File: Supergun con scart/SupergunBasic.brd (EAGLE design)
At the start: 114.9 x 67.3 mm, 37 parts, among them J1 AUDIO_JACK_3.5MM_PTH, X2 SCART-F

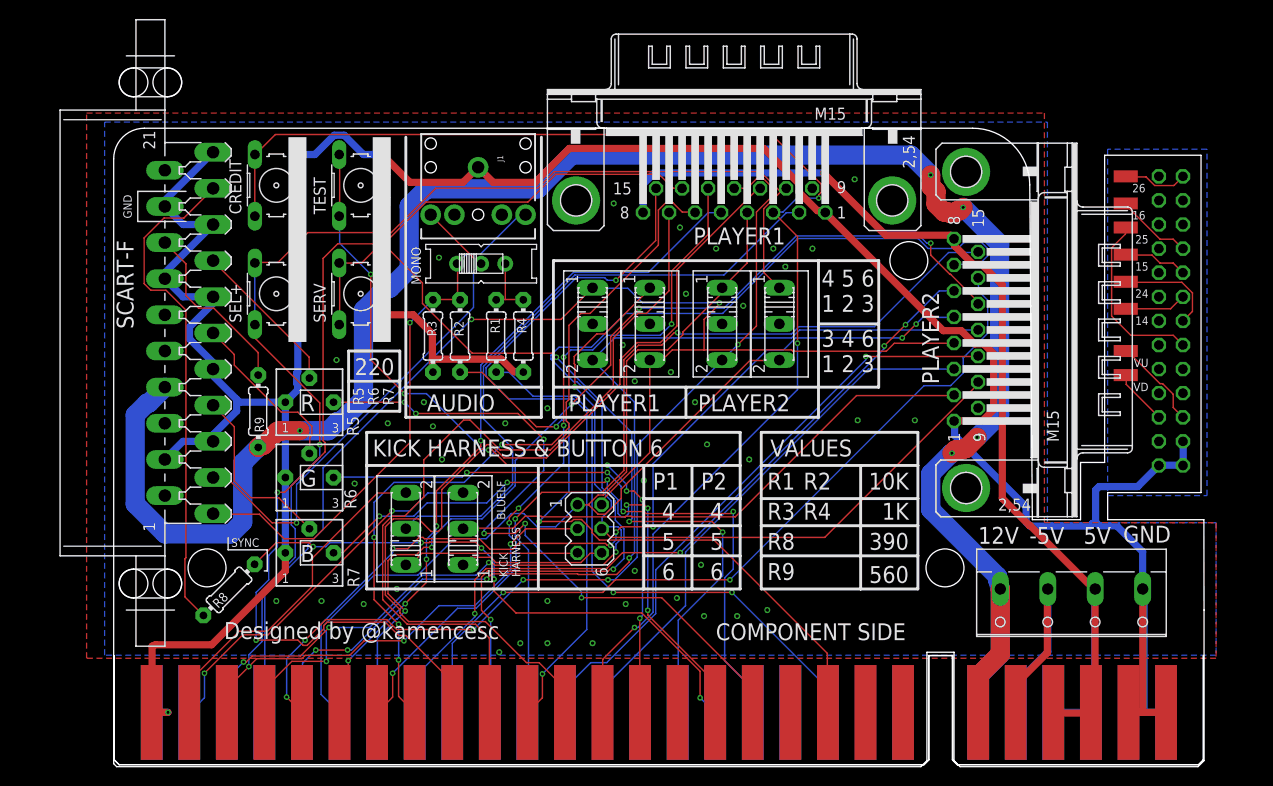
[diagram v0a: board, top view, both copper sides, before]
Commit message: Add files via upload
Actualizados sch y brd.

En el esquema se han icluïdo 2 subplacas que tienen que cortarse. Estas subplacas permiten conectarse al Kick Harness de CPS2. La pequeña va conectada a la Supergun (simplemente hacer coincidir los 2 circulos dibujados en una esquita del pinheader) y el grande va al connector Kick Harness de CPS2. Este incluye Vol+ y Vol- pero la supergun no se ha dado compatibilidad, por lo tanto estan para poder cablearos a unos swtich externos. Para usarlo simplemente asegurarse que el pin que señala la flecha es el de abajo la derecha al enchufarlo.
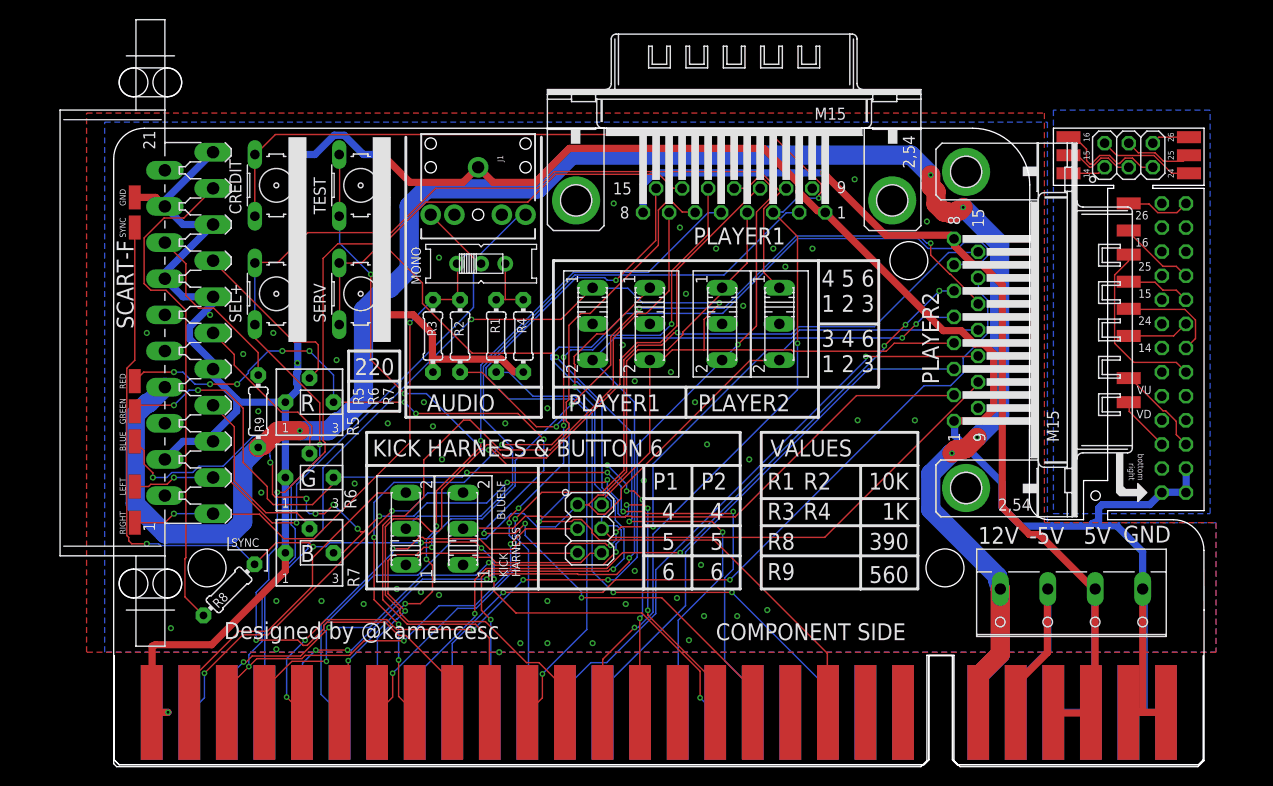
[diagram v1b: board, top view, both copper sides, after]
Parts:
- removed KH_CPS2: (no value), con-lstb:MA03-2
- added 1, 2, 3, 4, 5, 6, PAD1, PAD2, PAD3, PAD4, PAD5, PAD7, PAD8: (no value), wirepad:SMD1,27-2,54
- added JP2, JP3: (no value), pinhead:2X03
- moved JP1 2.88 mm to (111.8, 44.1)
- moved 15 2.88 mm to (107.0, 51.1)
- moved 16 2.88 mm to (107.0, 56.5)
- moved 24 2.88 mm to (107.0, 48.3)
- moved 25 2.88 mm to (107.0, 54.0)
- moved VD 2.88 mm to (107.0, 38.4)
- moved 14 2.88 mm to (107.0, 45.4)
- moved 26 2.88 mm to (107.0, 59.4)
- moved VU 2.88 mm to (107.0, 41.0)
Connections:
- new net K_14: 1.1, JP2.1
- new net K_15: 2.1, JP2.3
- new net K_16: 3.1, JP2.5
- new net K_24: 6.1, JP2.2
- new net K_25: 5.1, JP2.4
- new net K_26: 4.1, JP2.6
- net AUDIO_LEFT: now also PAD7.1
- net AUDIO_RIGHT: now also PAD8.1
- net GND: now also PAD5.1
- net J_BLUE: now also PAD3.1
- net J_GREEN: now also PAD2.1
- net J_RED: now also PAD1.1
- net J_SYNC: now also PAD4.1
- net K_P1_B6: now also JP3.5; no longer KH_CPS2.5
- net K_P2_B6: now also JP3.6; no longer KH_CPS2.6
- net P1_B4: now also JP3.1; no longer KH_CPS2.1
- net P1_B5: now also JP3.3; no longer KH_CPS2.3
- net P2_B4: now also JP3.2; no longer KH_CPS2.2
- net P2_B5: now also JP3.4; no longer KH_CPS2.4
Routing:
- net J_SYNC: track 60.8 -> 108.6 mm, vias 5 -> 6
- net J_BLUE: track 65.4 -> 102.8 mm, vias 6 -> 12
- net J_GREEN: track 68.5 -> 101.0 mm, vias 4 -> 6
- net J_RED: track 75.9 -> 103.2 mm, vias 6 -> 11
- net K_16: track 0.00 -> 12.1 mm
- net K_24: track 0.00 -> 10.2 mm
- net AUDIO_RIGHT: track 58.4 -> 67.1 mm, vias 1 -> 2
- net AUDIO_LEFT: track 53.7 -> 62.3 mm, vias 1 -> 2
- net K_15: track 0.00 -> 7.68 mm
- net K_25: track 0.00 -> 7.40 mm
- net K_26: track 0.00 -> 4.07 mm
- net K_14: track 0.00 -> 4.07 mm
- net GND: track 350.1 -> 352.3 mm, vias 44 -> 57
- net S_RED: track 16.6 -> 18.7 mm
- net P1_B2: track 74.8 -> 76.2 mm
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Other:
- outline, holes or cut-outs redrawn
- board text added: "14"
- board text added: "15"
- board text added: "16"
- board text added: "24"
- board text added: "25"
- board text added: "26"
- board text added: "BLUE"
- board text added: "Basic Supergun + Scart v 0.1 test"
- board text added: "GREEN"
- board text added: "LEFT"
- board text added: "RED"
- board text added: "RIGHT"
- board text added: "This side faces to the board"
- board text added: "bottom"
- board text added: "right"
- board text removed: "Basic Supergun"

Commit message: Add files via upload
Actualización
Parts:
- removed MO_ST: (no value), adafruit:EG1218
- removed PAD1, PAD2, PAD3, PAD4, PAD5, PAD7, PAD8: (no value), wirepad:SMD1,27-2,54
- removed S2, S3, S5, S6: (no value), switch:255SB
- removed X2: SCART-F, con-hirschmann:SCART-F
- added AUDIO, SYNC_G: (no value), con-wago-500:W237-102
- added JP4: (no value), pinhead:1X03
- added R10: (no value), bourns:3362P
- added RGB: (no value), con-wago-500:W237-103
- added S10, S11, S12, S8, S9: (no value), SparkFun-Switches:SWITCH_SPDT_PTH_11.6X4.0MM
- added U$1: SCART_F, scart:SCART_F
- S1, S4: device switch:255SB -> SparkFun-Switches:SWITCH_SPDT_PTH_11.6X4.0MM
- moved R9 83.8 mm to (98.9, 33.0)
- moved PLAYER_2 83.3 mm to (7.62, 32.5), turned to 270 degrees
- moved R7 77.6 mm to (95.9, 41.6)
- moved SEL+ 75.3 mm to (92.4, 51.6), turned to 180 degrees
- moved R6 67.0 mm to (86.7, 41.6)
- moved R5 56.9 mm to (77.5, 41.6)
- moved TEST 56.7 mm to (81.9, 51.6), turned to 180 degrees
- moved CREDIT 55.5 mm to (71.8, 51.6), turned to 180 degrees
- moved S4 54.3 mm to (19.2, 27.8), turned to 180 degrees
- moved R8 53.2 mm to (60.0, 41.9)
- moved S1 53.2 mm to (14.4, 27.8), turned to 180 degrees
- moved 26 47.6 mm to (59.4, 59.8), turned to 0 degrees
- moved 16 45.2 mm to (61.9, 59.8), turned to 0 degrees
- moved PLAYER_1 44.8 mm to (20.6, 59.5)
- moved JP1 42.5 mm to (74.5, 64.5), turned to 180 degrees
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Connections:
- removed net N$1: R8.1, X2.19
- removed net N$11: JAMMA1.11
- removed net N$3: MO_ST.S, R1.1, R4.2
- removed net N$4: R9.2, X2.16
- removed net N$5: JAMMA2.M
- removed net P1_B6: PLAYER_1.2, S2.2
- removed net P2_B6: PLAYER_2.2, S3.2
- new net DIRECT_SYNC: JP4.2, SYNC_G.1
- new net P_SYNC: JP4.3, R10.2, R8.2
- new net SCART_FAST_SW: R9.2, U$1.16
- new net SCART_SYNC: R8.1, U$1.19
- new net STR_LEFT: R1.1, R4.2, S8.3
- new net SW1_B6: PLAYER_1.2, S1.2
- new net SW2_B6: PLAYER_2.2, S4.2
- net AUDIO_LEFT: now also AUDIO.1, S8.2, U$1.3; no longer MO_ST.P, PAD7.1, X2.3
- net AUDIO_RIGHT: now also AUDIO.2, S8.1, U$1.1; no longer MO_ST.O, PAD8.1, X2.1
- net GND: now also R10.1, SYNC_G.2, U$1.13, U$1.14, U$1.17, U$1.18, U$1.21, U$1.4, U$1.5, U$1.9; no longer PAD5.1, X2.13, X2.14, X2.17, X2.18, X2.21, X2.4, X2.5, X2.9
- net J_BLUE: now also RGB.1; no longer PAD3.1
- net J_GREEN: now also RGB.2; no longer PAD2.1
- net J_P1_B6: now also S1.3; no longer S2.3
- net J_P2_B6: now also S4.3; no longer S3.3
- net J_RED: now also RGB.3; no longer PAD1.1
- net J_SYNC: now also JP4.1, R10.3; no longer PAD4.1, R8.2
- net K_P1_B6: now also S1.1; no longer S2.1
- net K_P2_B6: now also S4.1; no longer S3.1
- net P1_B3: now also S9.3; no longer S1.3
- net P1_B4: now also S12.3, S9.1; no longer PLAYER_1.4, S1.1, S4.3
- net P1_B5: now also S12.1; no longer PLAYER_1.10, S4.1
- net P2_B3: now also S11.3; no longer S5.3
- net P2_B4: now also S10.3, S11.1; no longer PLAYER_2.4, S5.1, S6.3
- net P2_B5: now also S10.1; no longer PLAYER_2.10, S6.1
- net SW1_B4: now also PLAYER_1.4, S9.2; no longer S1.2
- net SW1_B5: now also PLAYER_1.10, S12.2; no longer S4.2
- net SW2_B4: now also PLAYER_2.4, S11.2; no longer S5.2
- net SW2_B5: now also PLAYER_2.10, S10.2; no longer S6.2
- net S_BLUE: now also U$1.7; no longer X2.7
- net S_GREEN: now also U$1.11; no longer X2.11
- net S_RED: now also U$1.15; no longer X2.15
- net VCC+12: now also U$1.8; no longer X2.8
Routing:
- net VCC+12: track 212.5 -> 90.9 mm, vias 5 -> 0
- net P2_B5: track 133.4 -> 59.3 mm, vias 5 -> 3
- net P2_B4: track 134.6 -> 66.3 mm, vias 2 -> 4
- net P1_B6: track 66.9 -> 0.00 mm
- net P2_DOWN: track 112.2 -> 47.9 mm
- net GND: track 352.3 -> 416.2 mm, vias 57 -> 3
- net J_SYNC: track 108.6 -> 48.7 mm, vias 6 -> 2
- net P2_B2: track 96.1 -> 37.6 mm, vias 6 -> 3
- net J_RED: track 103.2 -> 44.9 mm, vias 11 -> 0
- net P2_B1: track 102.1 -> 44.3 mm, vias 5 -> 3
- net P2_B6: track 57.7 -> 0.00 mm
- net VCC: track 117.6 -> 172.8 mm, vias 1 -> 7
- net AUDIO_RIGHT: track 67.1 -> 120.7 mm, vias 2 -> 1
- net P1_B4: track 116.3 -> 63.3 mm, vias 1 -> 4
- net N$1: track 52.9 -> 0.00 mm
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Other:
- outline, holes or cut-outs redrawn
- board text added: "500"
- board text added: "B4"
- board text added: "B5"
- board text added: "Basic Supergun + Scart V0.2"
- board text added: "COMPONENTS SIDE"
- board text added: "Faces to the PCB"
- board text added: "JAMMA SYNC"
- board text added: "L"
- board text added: "POT SYNC"
- board text added: "R10"
- board text added: "bottom right"
- board text removed: "BLUE"
- board text removed: "Basic Supergun + Scart v 0.1 test"
- board text removed: "COMPONENT SIDE"
- board text removed: "GREEN"
- board text removed: "LEFT"
- board text removed: "RED"
- board text removed: "RIGHT"
- board text removed: "This side faces to the board"
- board text removed: "bottom"
- board text removed: "right"

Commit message: Add files via upload
Minor changes
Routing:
- net P1_START: track 68.7 -> 69.4 mm

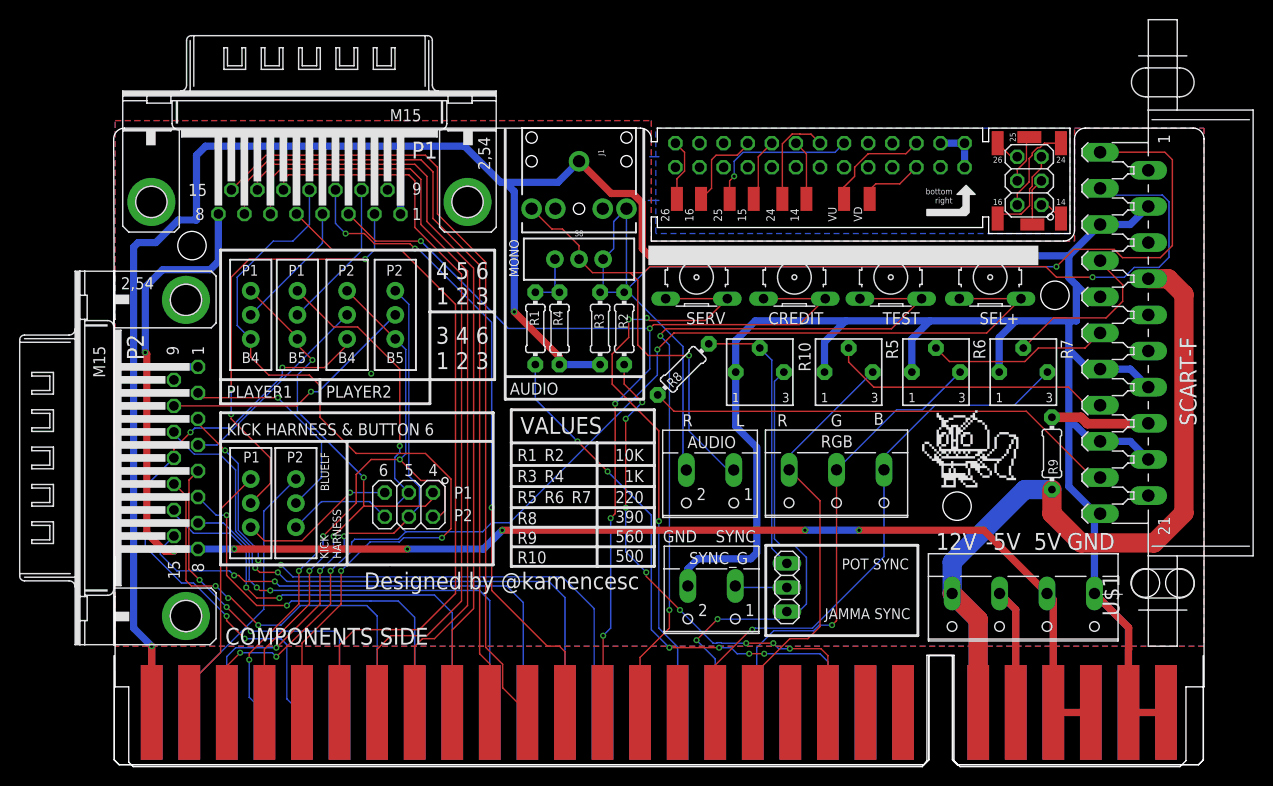
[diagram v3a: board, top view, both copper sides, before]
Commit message: Add files via upload
Optional LM1881 to scart connector, now you can select between lm1881 or jamma sync

LED added

Other improvements
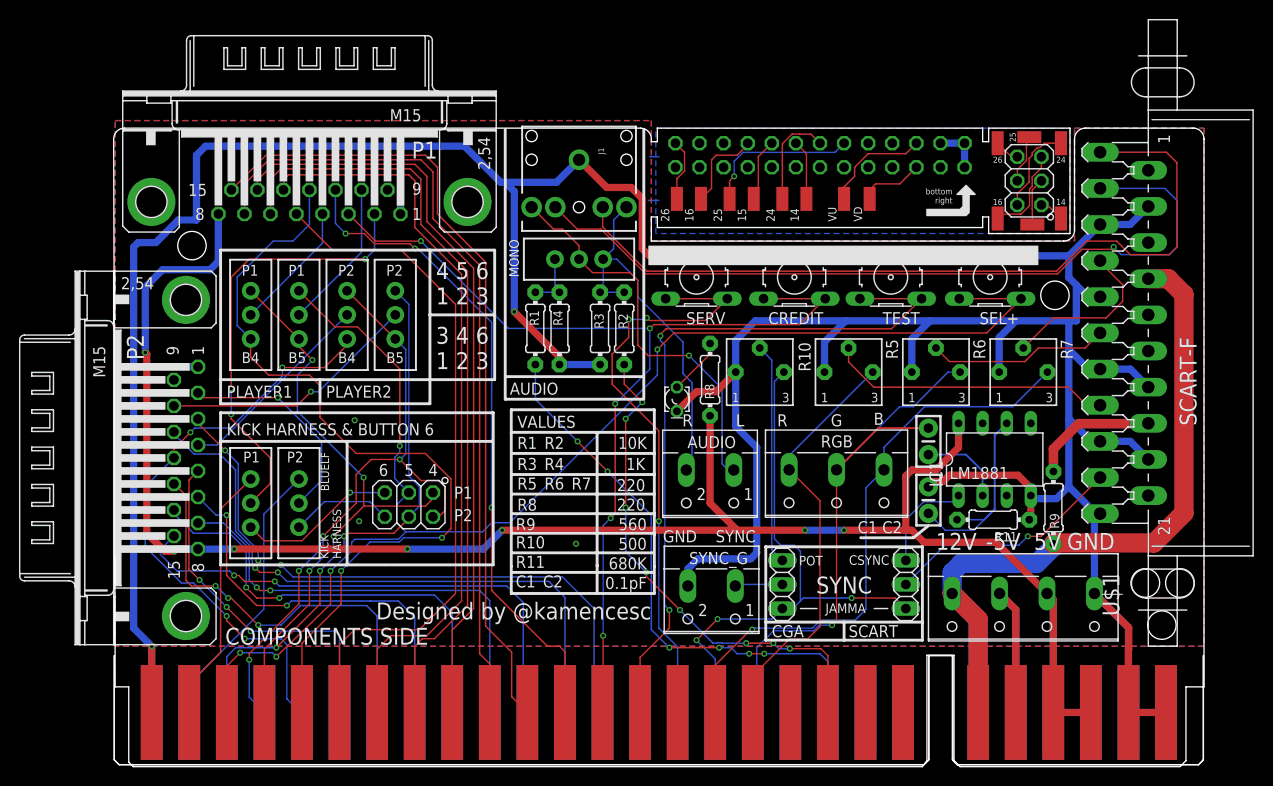
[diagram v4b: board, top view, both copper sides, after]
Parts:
- added C1, C2: 0.1uF, SparkFun-Capacitors:CAP-PTH-SMALL-KIT
- added IC1: LM1881N, oldchips2:DIL08
- added JP5: (no value), pinhead:1X03
- added LED1: (no value), led:LD260
- added R11: 680k, adafruit:0204/7
- R8: value 390 -> 220
- moved R9 5.72 mm to (99.1, 27.3)
- moved R8 3.03 mm to (62.9, 40.8), turned to 90 degrees
- moved JP4 0.57 mm to (70.5, 19.2)
- moved S4 0.32 mm to (19.5, 27.8)
- moved S12 0.16 mm to (19.5, 47.6)
- moved J1 0.16 mm to (49.1, 64.0)
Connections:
- new net A_LEFT_OUT: J1.TSH, U$1.3
- new net A_RIGHT_OUT: J1.RSH, U$1.1
- new net C_SYNC: IC1.1, JP5.3
- new net N$2: LED1.A, R8.2
- new net N$4: C2.1, IC1.6, R11.2
- new net N$5: C1.2, IC1.2
- new net VSYNC: IC1.3
- net AUDIO_LEFT: no longer U$1.3
- net AUDIO_RIGHT: no longer U$1.1
- net GND: now also C2.2, IC1.4, LED1.K, R11.1
- net J_GREEN: now also C1.1
- net J_SYNC: now also JP5.1
- net P_SYNC: no longer R8.2
- net SCART_SYNC: now also JP5.2; no longer R8.1
- net VCC: now also IC1.8, R8.1
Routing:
- net A_RIGHT_OUT: track 0.00 -> 84.2 mm
- net A_LEFT_OUT: track 0.00 -> 83.8 mm, vias 0 -> 1
- net AUDIO_RIGHT: track 120.7 -> 39.8 mm, vias 1 -> 0
- net AUDIO_LEFT: track 114.3 -> 42.3 mm, vias 2 -> 1
- net VCC: track 172.8 -> 201.1 mm
- net GND: track 416.2 -> 444.4 mm, vias 3 -> 5
- net SCART_SYNC: track 50.2 -> 25.1 mm, vias 0 -> 1
- net N$4: track 0.00 -> 21.0 mm
- net J_GREEN: track 49.8 -> 61.3 mm
- net C_SYNC: track 0.00 -> 10.9 mm
- net J_SYNC: track 48.7 -> 59.3 mm, vias 2 -> 3
- net N$5: track 0.00 -> 9.01 mm
- net VCC+12: track 90.9 -> 84.3 mm
- net P_SYNC: track 29.4 -> 23.4 mm
- net N$2: track 0.00 -> 6.05 mm
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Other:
- board text added: "0.1pF"
- board text added: "680K"
- board text added: "C1"
- board text added: "C1 C2"
- board text added: "C2"
- board text added: "CGA"
- board text added: "CSYNC"
- board text added: "JAMMA"
- board text added: "LM1881"
- board text added: "POT"
- board text added: "R11"
- board text added: "SCART"
- board text removed: "390"
- board text removed: "JAMMA SYNC"
- board text removed: "POT SYNC"

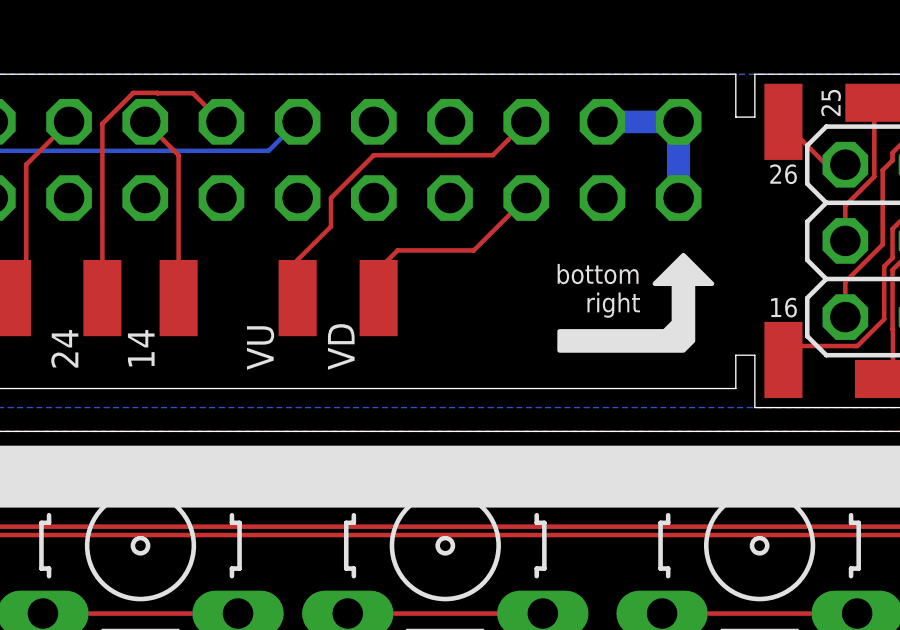
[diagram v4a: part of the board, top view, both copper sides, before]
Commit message: Add files via upload
GND pad on the Kick Harness
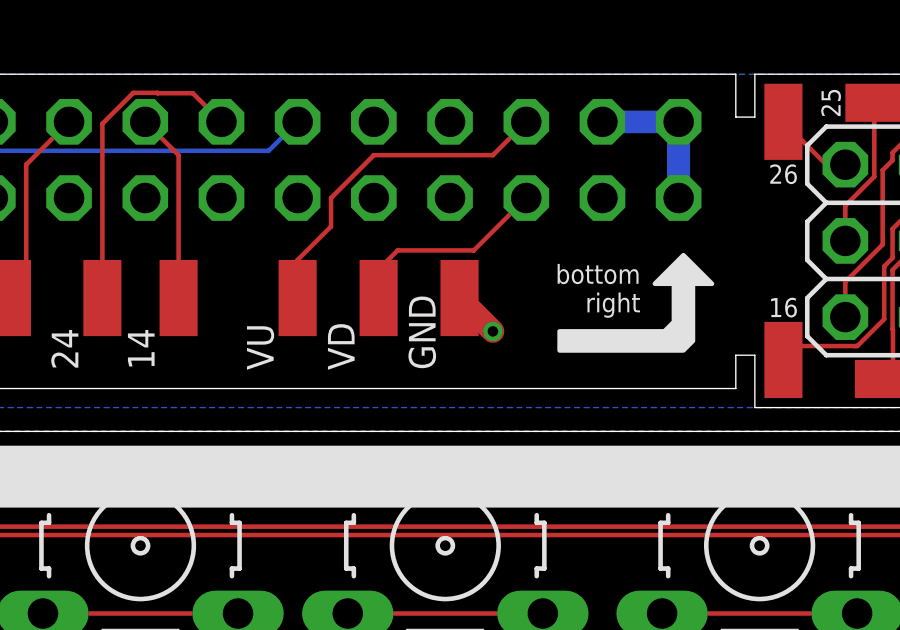
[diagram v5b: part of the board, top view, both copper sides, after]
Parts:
- added GND: (no value), wirepad:SMD1,27-2,54
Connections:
- net GND: now also GND.1
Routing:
- net GND: track 444.4 -> 446.0 mm, vias 5 -> 6
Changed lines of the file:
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@@
 <attribute name="VALUE" x="86.6775" y="15.39875" size="1.27" layer="27" rot="R90"/>
+</element>
+<element name="GND" library="wirepad" library_urn="urn:adsk.eagle:library:412" package="SMD1,27-2,54" package3d_urn="urn:adsk.eagle:package:30839/1" value="" x="82.39125" y="59.84875" smashed="yes">
+<attribute name="NAME" x="81.59125" y="57.44875" size="0.889" layer="25" rot="R90"/>
+<attribute name="VALUE" x="82.39125" y="59.84875" size="0.0254" layer="27"/>
 </element>
 </elements>
@@
 <wire x1="96.67875" y1="28.575" x2="96.67875" y2="26.19375" width="0.762" layer="1"/>
 <wire x1="96.67875" y1="26.19375" x2="96.52" y2="26.035" width="0.762" layer="1"/>
+<contactref element="GND" pad="1"/>
+<wire x1="82.39125" y1="59.84875" x2="83.5025" y2="58.7375" width="0.762" layer="1"/>
+<via x="83.5025" y="58.7375" extent="1-16" drill="0.35"/>
 </signal>
 <signal name="J_P2_B6">
